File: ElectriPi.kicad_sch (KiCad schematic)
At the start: 34 parts

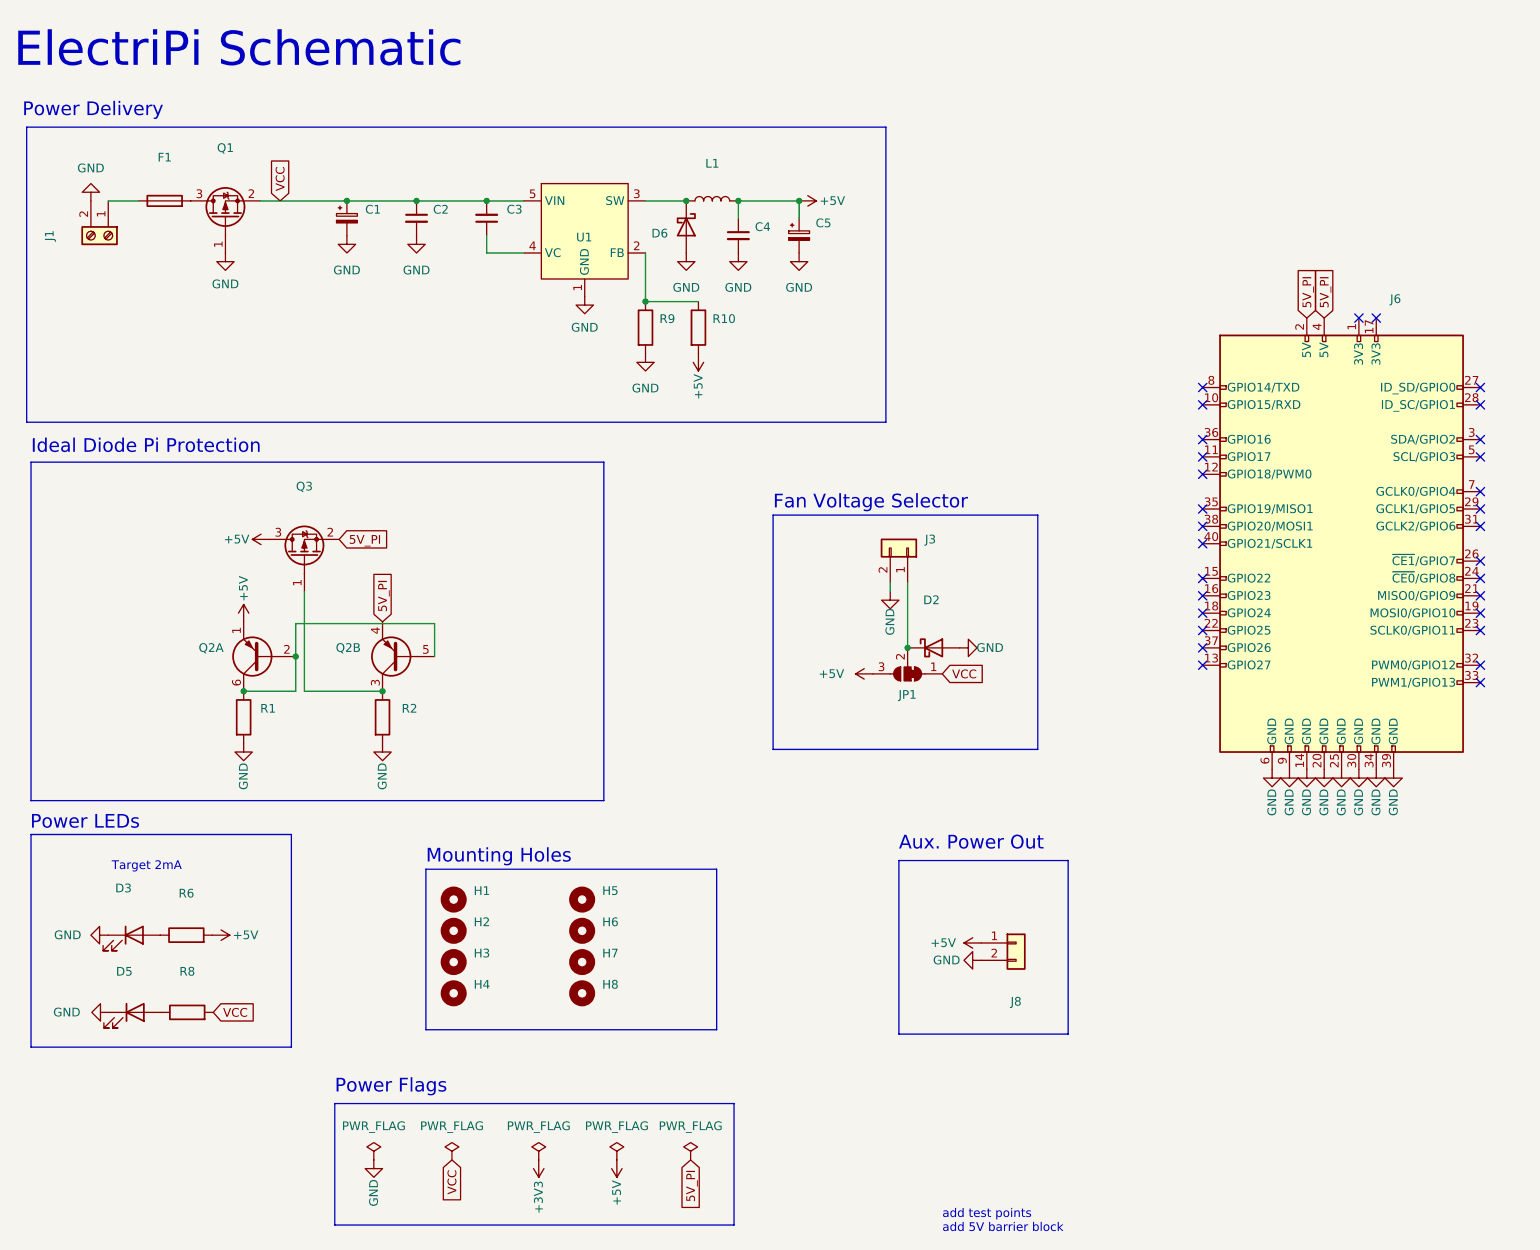
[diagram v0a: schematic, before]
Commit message: Bladefuse holder switched to Littelfuse nano 2 fuse holder
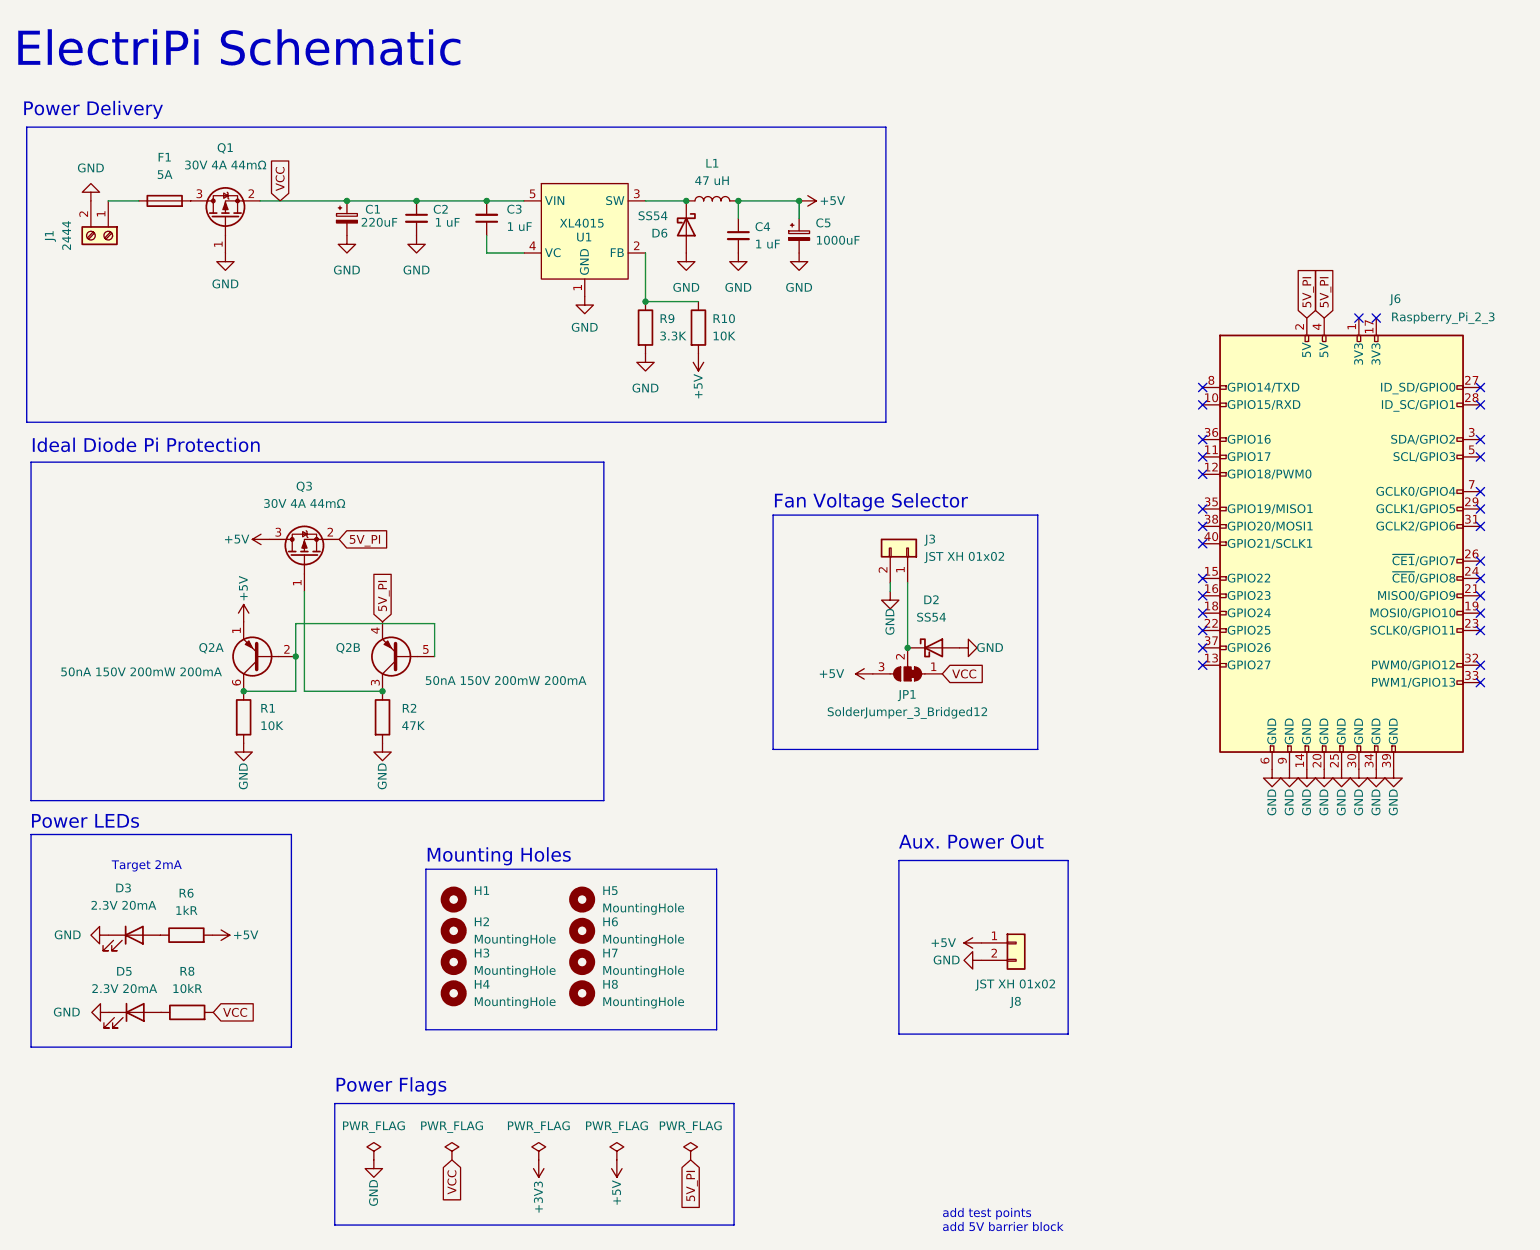
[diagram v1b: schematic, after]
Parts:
- C1: value (none) -> 220uF; footprint (none) -> Capacitor_SMD:CP_Elec_10x10
- C2, C3, C4: value (none) -> 1 uF; footprint (none) -> Capacitor_SMD:C_0603_1608Metric
- C5: value (none) -> 1000uF; footprint (none) -> Capacitor_SMD:CP_Elec_8x10
- D2, D6: value (none) -> SS54; footprint (none) -> Diode_SMD:D_SMA
- D3, D5: value (none) -> 2.3V 20mA; footprint (none) -> LED_SMD:LED_0603_1608Metric
- F1: value (none) -> 5A
- H2, H3, H4: value (none) -> MountingHole; footprint (none) -> MountingHole:MountingHole_2.7mm_M2.5_DIN965_Pad
- H5, H6, H7, H8: value (none) -> MountingHole; footprint (none) -> MountingHole:MountingHole_3.5mm
- J1: value (none) -> 2444; footprint (none) -> TerminalBlock_4Ucon:TerminalBlock_4Ucon_1x02_P3.50mm_Horizontal
- J3, J8: value (none) -> JST XH 01x02; footprint (none) -> Connector_JST:JST_XH_B2B-XH-A_1x02_P2.50mm_Vertical
- J6: value (none) -> Raspberry_Pi_2_3; footprint (none) -> Connector_PinSocket_2.54mm:PinSocket_2x20_P2.54mm_Vertical
- JP1: value (none) -> SolderJumper_3_Bridged12; footprint (none) -> Jumper:SolderJumper-3_P1.3mm_Bridged2Bar12_RoundedPad1.0x1.5mm
- L1: value (none) -> 47 uH; footprint (none) -> Inductor_SMD:L_12x12mm_H6mm
- Q1, Q3: value (none) -> 30V 4A 44mΩ; footprint (none) -> Package_TO_SOT_SMD:SOT-23
- Q2: value (none) -> 50nA 150V 200mW 200mA; footprint (none) -> Package_TO_SOT_SMD:SOT-363_SC-70-6
- R1: value (none) -> 10K; footprint (none) -> Resistor_SMD:R_0402_1005Metric
- R10: value (none) -> 10K; footprint (none) -> Resistor_SMD:R_0603_1608Metric
- R2: value (none) -> 47K; footprint (none) -> Resistor_SMD:R_0402_1005Metric
- R6: value (none) -> 1kR; footprint (none) -> Resistor_SMD:R_0402_1005Metric
- R8: value (none) -> 10kR; footprint (none) -> Resistor_SMD:R_0402_1005Metric
- R9: value (none) -> 3.3K; footprint (none) -> Resistor_SMD:R_0603_1608Metric
- U1: value (none) -> XL4015; footprint (none) -> Package_TO_SOT_SMD:TO-263-5_TabPin3

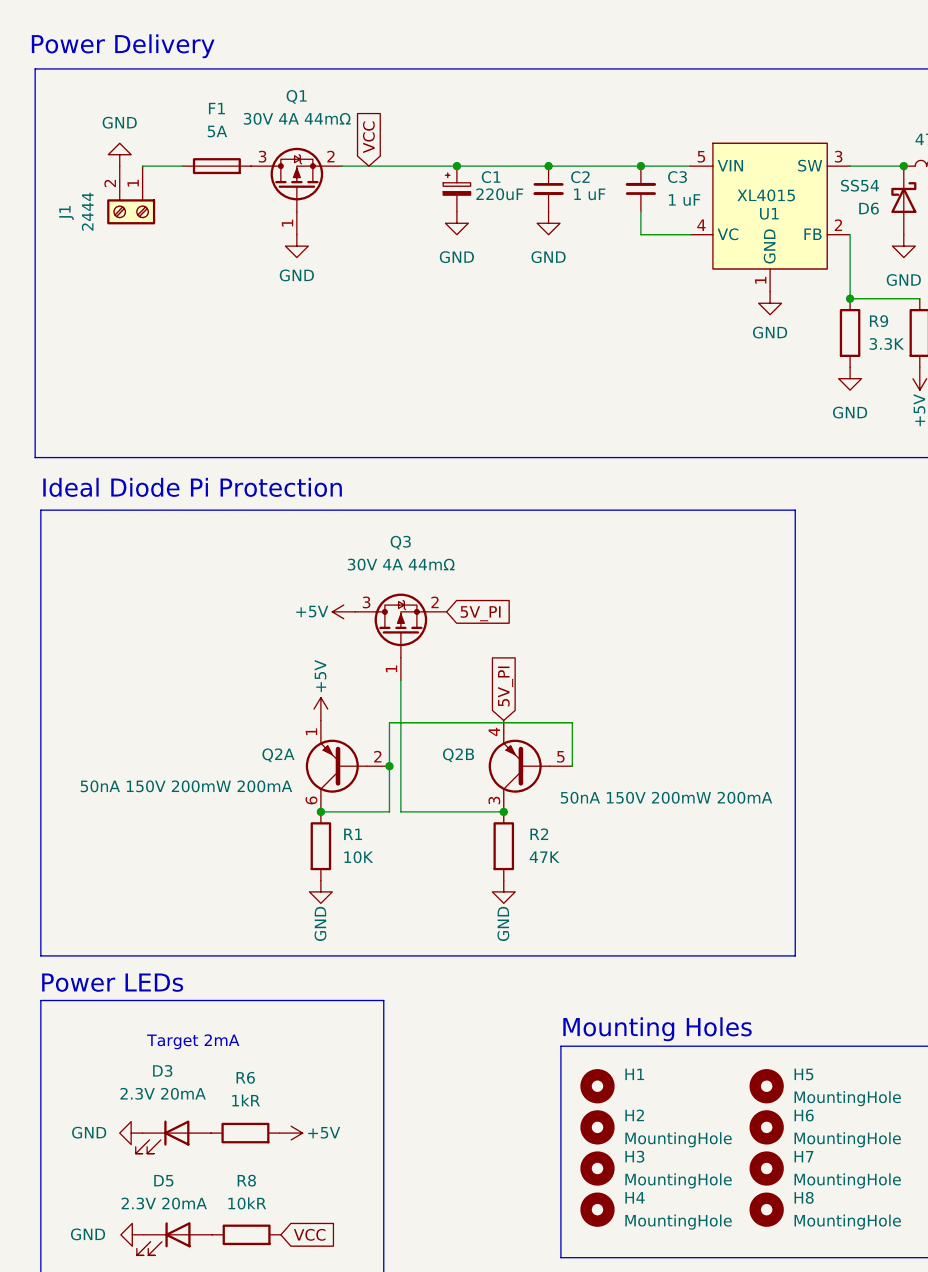
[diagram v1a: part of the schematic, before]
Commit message: F.Silk, Fan passthough, Fuse, XH input and designator changes
- Added more pin notes to 40Pin GPIO
- Added cutout to fan hole to allow passthrough from reverse mounting
- customised F1 Littelfuse footprint to correctly suit NANO 2 footprint
- Add JST XH Input Option
- Moved superfluous reference designators to hidden layer (user2)
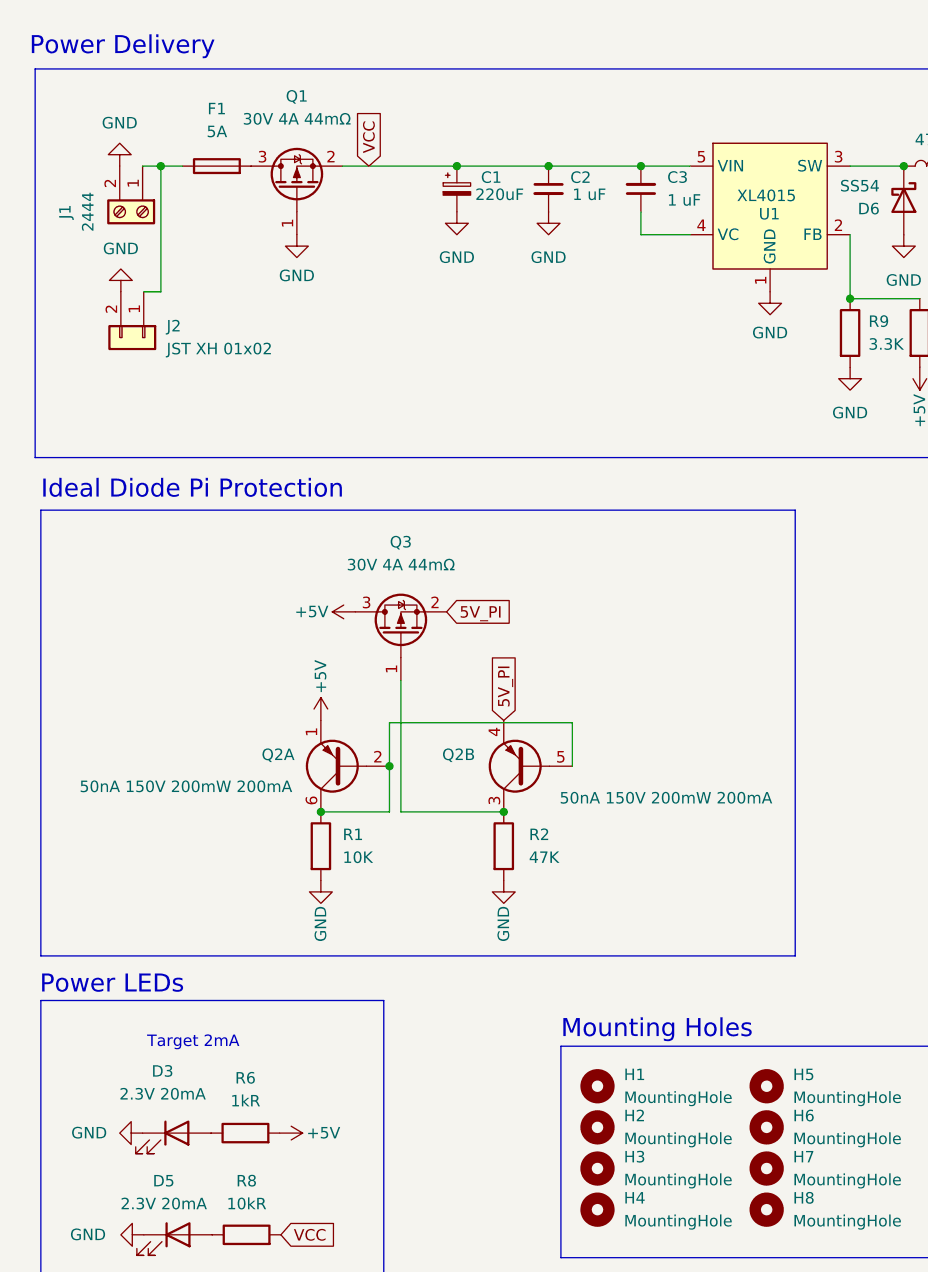
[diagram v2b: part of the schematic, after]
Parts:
- added J2: JST XH 01x02, Connector_JST:JST_XH_B2B-XH-A_1x02_P2.50mm_Vertical, symbol Connector_Generic:Conn_01x02
- F1: footprint (none) -> Fuse:Fuse_Littelfuse-NANO2-451_453; LCSC (none) -> C108518; ManfNum Keystone 3568 -> (none)
- H1: value (none) -> MountingHole; footprint (none) -> MountingHole:MountingHole_2.7mm_M2.5_DIN965_Pad
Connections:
- net GND: now also J2.2 (Pin_2)
- net at F1.1, J1.1 (Pin_1): now also J2.1 (Pin_1)
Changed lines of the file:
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@@
   (junction (at 84.455 43.18) (diameter 0) (color 0 0 0 0)
+  )
+  (junction (at 31.115 43.18) (diameter 0) (color 0 0 0 0)
   )
   (junction (at 74.1934 43.18) (diameter 0) (color 0 0 0 0)
@@
     (stroke (width 0) (type default) (color 0 0 0 0))
   )
-  (wire (pts (xy 29.083 43.18) (xy 33.528 43.18))
+  (wire (pts (xy 31.115 43.18) (xy 33.528 43.18))
+    (stroke (width 0) (type default) (color 0 0 0 0))
+  )
+  (wire (pts (xy 29.083 43.18) (xy 31.115 43.18))
     (stroke (width 0) (type default) (color 0 0 0 0))
   )
@@
     (stroke (width 0) (type default) (color 0 0 0 0))
   )
+  (wire (pts (xy 31.115 57.15) (xy 31.115 43.18))
+    (stroke (width 0) (type default) (color 0 0 0 0))
+  )
   (wire (pts (xy 107.696 43.18) (xy 113.665 43.18))
     (stroke (width 0) (type default) (color 0 0 0 0))
@@
   )
   (polyline (pts (xy 118.11 140.97) (xy 118.11 164.465))
+    (stroke (width 0) (type default) (color 0 0 0 0))
+  )
+  (wire (pts (xy 29.21 57.15) (xy 31.115 57.15))
     (stroke (width 0) (type default) (color 0 0 0 0))
   )
@@
     (pin "2")
   )
+  (symbol (lib_id "power:GND") (at 26.67 57.15 180) (unit 1)
+    (in_bom yes) (on_board yes) (fields_autoplaced)
+    (property "Reference" "#PWR09" (id 0) (at 26.67 50.8 0)
+      (effects (font (size 1.27 1.27)) hide)
+    )
+    (property "Value" "GND" (id 1) (at 26.67 52.3748 0))
+    (property "Footprint" "" (id 2) (at 26.67 57.15 0)
+      (effects (font (size 1.27 1.27)) hide)
+    )
+    (property "Datasheet" "" (id 3) (at 26.67 57.15 0)
+      (effects (font (size 1.27 1.27)) hide)
+    )
+    (pin "1")
+  )
+  (symbol (lib_id "Connector_Generic:Conn_01x02") (at 29.21 62.23 270) (unit 1)
+    (in_bom yes) (on_board yes) (fields_autoplaced)
+    (property "Reference" "J2" (id 0) (at 31.75 60.9599 90)
+      (effects (font (size 1.27 1.27)) (justify left))
+    )
+    (property "Value" "JST XH 01x02" (id 1) (at 31.75 63.4999 90)
+      (effects (font (size 1.27 1.27)) (justify left))
+    )
+    (property "Footprint" "Connector_JST:JST_XH_B2B-XH-A_1x02_P2.50mm_Vertical" (id 2) (at 29.21 62.23 0)
+      (effects (font (size 1.27 1.27)) hide)
+    )
+    (property "Datasheet" "~" (id 3) (at 29.21 62.23 0)
+      (effects (font (size 1.27 1.27)) hide)
+    )
+    (pin "1")
+    (pin "2")
+  )
   (symbol (lib_id "Transistor_BJT:MMDT5401") (at 71.755 109.855 180) (unit 2)
     (in_bom yes) (on_board yes)
@@
     (property "Reference" "F1" (id 0) (at 37.338 36.83 90))
     (property "Value" "5A" (id 1) (at 37.338 39.37 90))
-    (property "Footprint" "" (id 2) (at 37.338 44.958 90)
+    (property "Footprint" "Fuse:Fuse_Littelfuse-NANO2-451_453" (id 2) (at 37.338 44.958 90)
       (effects (font (size 1.27 1.27)) hide)
     )
@@
       (effects (font (size 1.27 1.27)) hide)
     )
-    (property "LCSC" "" (id 4) (at 37.338 43.18 90)
+    (property "LCSC" "C108518" (id 4) (at 37.338 43.18 90)
       (effects (font (size 1.27 1.27)) hide)
     )
@@
       (effects (font (size 1.27 1.27)) hide)
     )
-    (property "ManfNum" "Keystone 3568" (id 7) (at 37.338 43.18 0)
+    (property "ManfNum" "" (id 7) (at 37.338 43.18 0)
       (effects (font (size 1.27 1.27)) hide)
     )
@@
       (effects (font (size 1.27 1.27)) (justify left))
     )
-    (property "Value" "" (id 1) (at 82.55 146.6849 0)
-      (effects (font (size 1.27 1.27)) (justify left))
-    )
-    (property "Footprint" "" (id 2) (at 79.629 145.415 0)
+    (property "Value" "MountingHole" (id 1) (at 82.55 146.6849 0)
+      (effects (font (size 1.27 1.27)) (justify left))
+    )
+    (property "Footprint" "MountingHole:MountingHole_2.7mm_M2.5_DIN965_Pad" (id 2) (at 79.629 145.415 0)
       (effects (font (size 1.27 1.27)) hide)
     )
@@
       (reference "#PWR08") (unit 1) (value "GND") (footprint "")
     )
+    (path "/8957aaae-c6d6-4f83-97ff-f71342f0b9ac"
+      (reference "#PWR09") (unit 1) (value "GND") (footprint "")
+    )
     (path "/e82c6728-328a-4fb4-b819-3d2b4377817e"
       (reference "#PWR011") (unit 1) (value "GND") (footprint "")
@@
       (reference "J1") (unit 1) (value "2444") (footprint "TerminalBlock_4Ucon:TerminalBlock_4Ucon_1x02_P3.50mm_Horizontal")
     )
+    (path "/933a4598-ee67-401d-bec6-d7278425186a"
+      (reference "J2") (unit 1) (value "JST XH 01x02") (footprint "Connector_JST:JST_XH_B2B-XH-A_1x02_P2.50mm_Vertical")
+    )
     (path "/12571268-be51-457b-85b9-1c2e7398dddd"
